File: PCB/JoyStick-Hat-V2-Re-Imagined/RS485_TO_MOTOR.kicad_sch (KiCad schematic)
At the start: 16 parts, among them J5 RJHSE-5381, U4 MAX3535ECWI+T

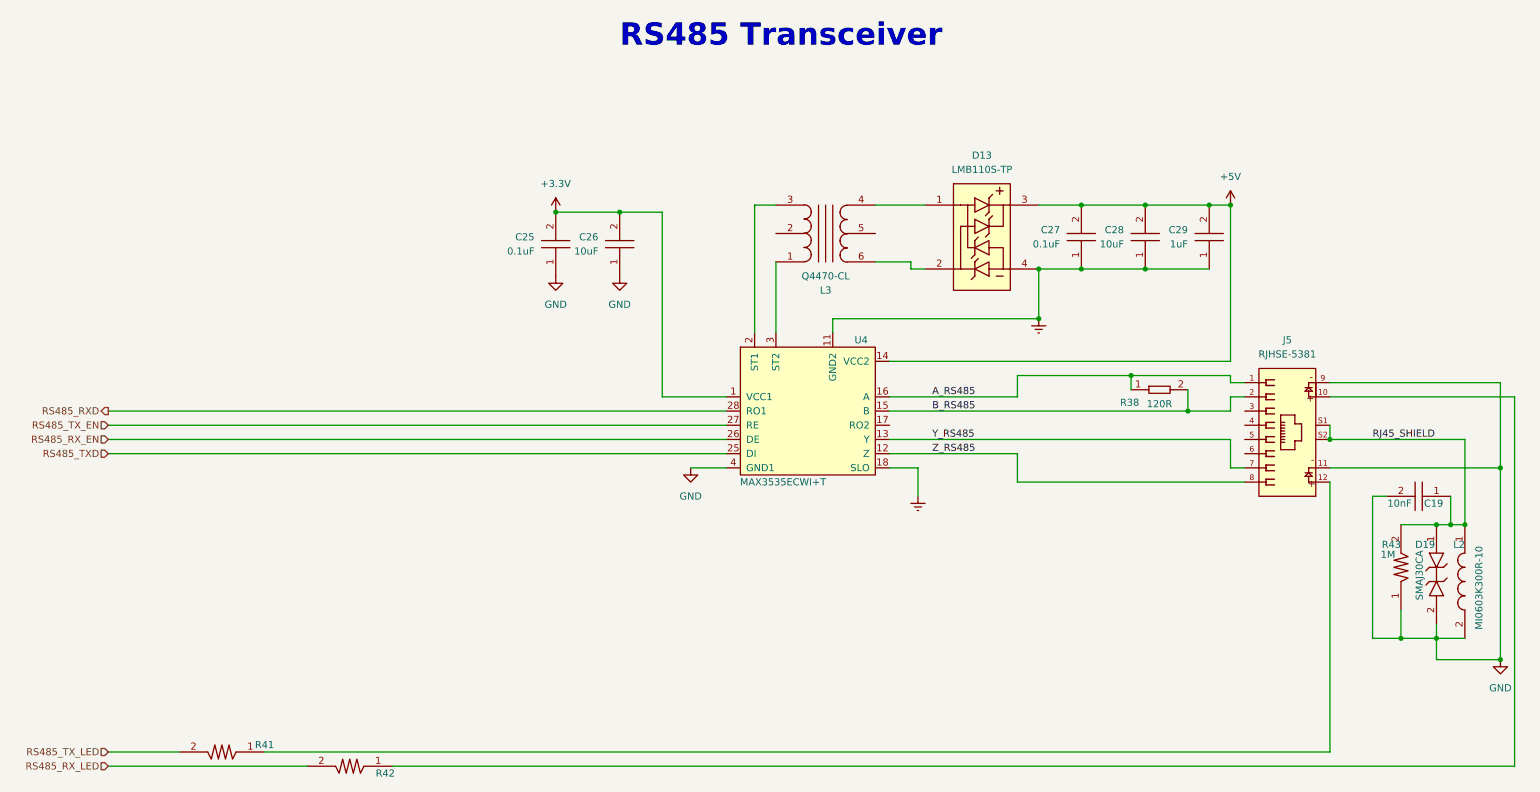
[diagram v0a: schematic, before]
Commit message: Daisy Chaining
Modified RS485 circuit with dual port connector for daisy chaining systems on the wheel chair !
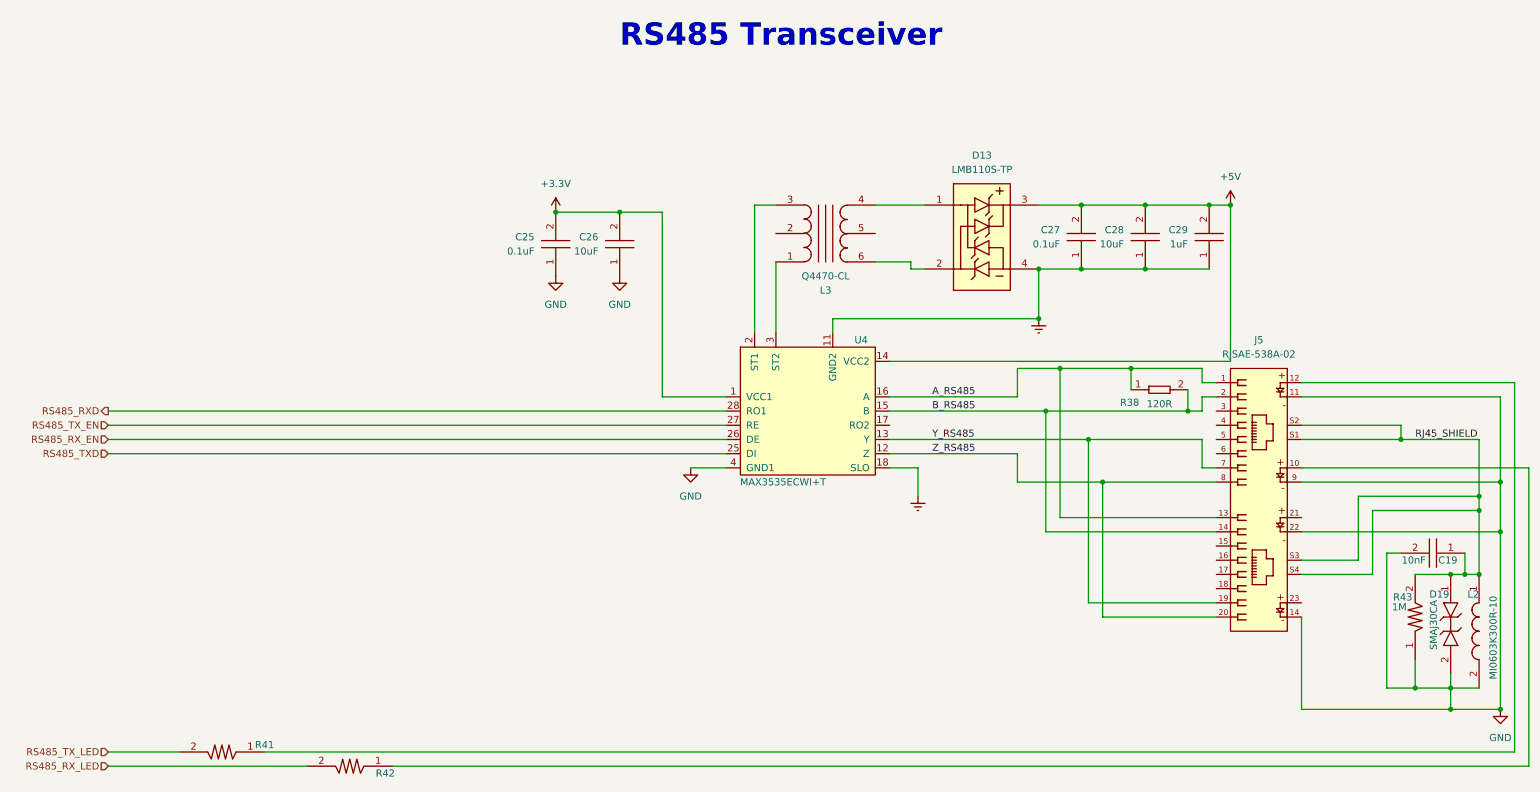
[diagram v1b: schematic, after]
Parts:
- removed J5: RJHSE-5381, AVR-KiCAD-Lib-Connectors:AMPHENOL_RJHSE-5381, symbol AVR-KiCAD-Lib-Connectors:RJHSE-5381
- added J5: RJSAE-538A-02, AVR-KiCAD-Lib-Connectors:AMPHENOL_RJSAE538A02, symbol AVR-KiCAD-Lib-Connectors:RJSAE-538A-02
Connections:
- net A_RS485: now also J5.1, J5.13
- net B_RS485: now also J5.14, J5.2
- net GND: now also J5.11, J5.14, J5.22, J5.9
- net RJ45_SHIELD: now also J5.S1, J5.S2, J5.S3, J5.S4
- net Y_RS485: now also J5.19, J5.7
- net Z_RS485: now also J5.20, J5.8
- net at R42.1: now also J5.10
- net at R41.1: now also J5.12
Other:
- moved on the sheet: C19, D19, L2, R43

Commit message: Fab Fixes
Fixing for Frabrication, DRC cleared by pending external review subject to change.
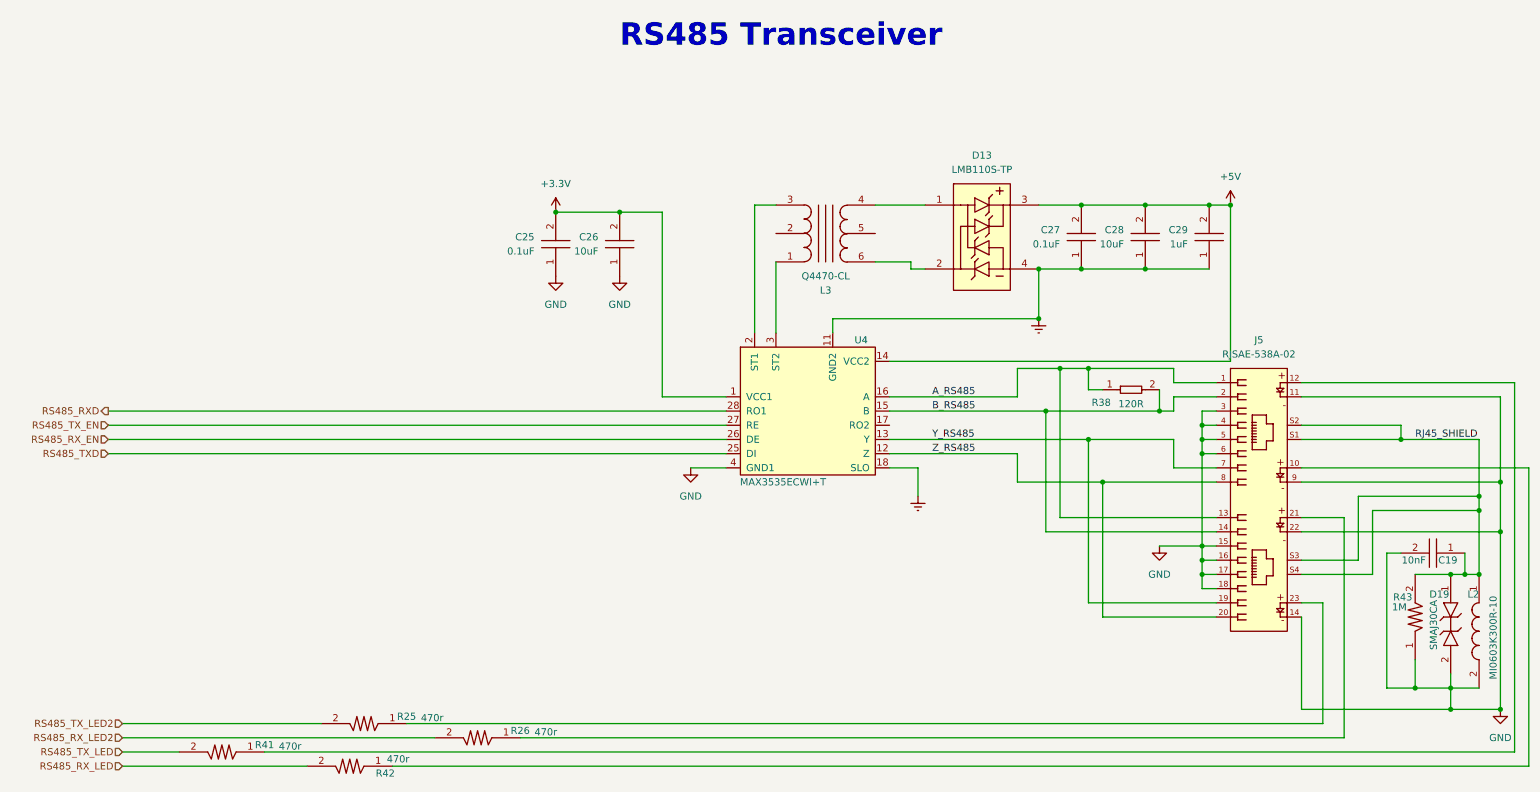
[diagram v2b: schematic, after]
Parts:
- added R25, R26: RC0603FR-07470RL, AVR-KiCAD-Lib-Resistors:R0603, symbol AVR-KiCAD-Lib-Resistors:RC0603FR-07470RL
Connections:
- net GND: now also J5.15, J5.16, J5.17, J5.18, J5.3, J5.4, J5.5, J5.6
- net at J5.21: now also R26.1
- net at J5.23: now also R25.1
- new net RS485_RX_LED2: R26.2
- new net RS485_TX_LED2: R25.2
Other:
- moved on the sheet: R38

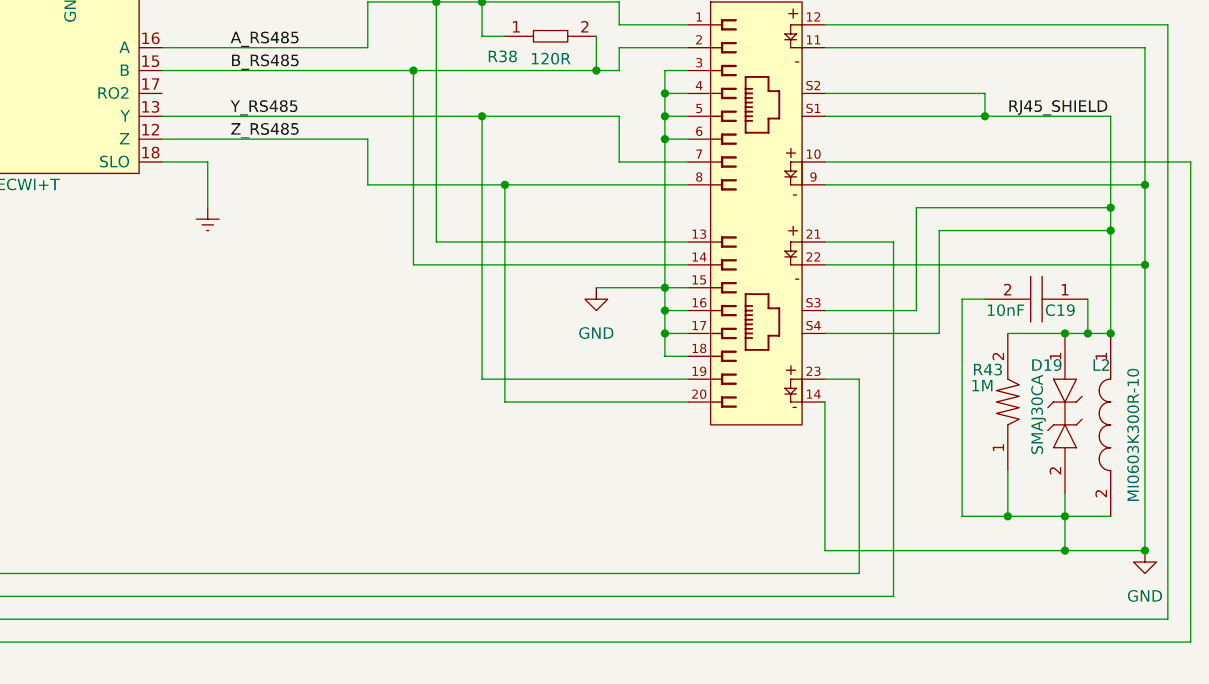
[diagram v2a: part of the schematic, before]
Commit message: RS485 Circuit Fixes, STM32 Expansion
Fixe RS485 circuit errors, changed PCB topology for RS485. Added STM32 expansion IO in place of 5V Regulator.
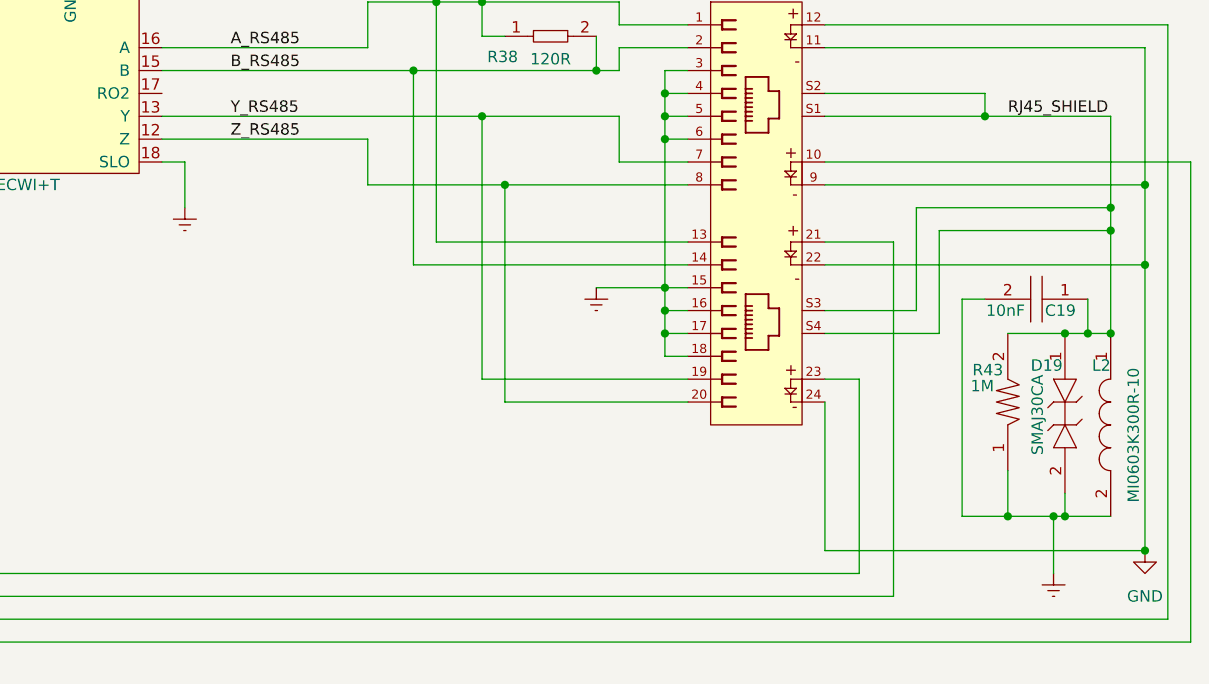
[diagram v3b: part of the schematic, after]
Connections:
- net Earth: now also C19.2, D19.2, J5.15, J5.16, J5.17, J5.18, J5.3, J5.4, J5.5, J5.6, L2.2, R43.1
- net GND: now also J5.24; no longer C19.2, D19.2, J5.14, J5.15, J5.16, J5.17, J5.18, J5.3, J5.4, J5.5, J5.6, L2.2, R43.1
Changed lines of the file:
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@@
 	)
 	(junction
+		(at 266.7 148.59)
+		(diameter 0)
+		(color 0 0 0 0)
+	)
+	(junction
 		(at 267.97 148.59)
 		(diameter 0)
@@
 	)
 	(junction
-		(at 267.97 152.4)
-		(diameter 0)
-		(color 0 0 0 0)
-	)
-	(junction
 		(at 119.38 63.5)
 		(diameter 0)
@@
 	(wire
 		(pts
-			(xy 241.3 152.4) (xy 267.97 152.4)
-		)
-		(stroke
-			(width 0)
-			(type default)
-		)
-	)
-	(wire
-		(pts
 			(xy 119.38 63.5) (xy 127 63.5)
 		)
@@
 	(wire
 		(pts
-			(xy 267.97 148.59) (xy 267.97 152.4)
-		)
-		(stroke
-			(width 0)
-			(type default)
-		)
-	)
-	(wire
-		(pts
 			(xy 213.36 62.23) (xy 224.79 62.23)
 		)
@@
 	(wire
 		(pts
-			(xy 167.64 109.22) (xy 172.72 109.22)
+			(xy 170.18 109.22) (xy 167.64 109.22)
 		)
 		(stroke
@@
 	(wire
 		(pts
-			(xy 267.97 148.59) (xy 261.62 148.59)
+			(xy 267.97 148.59) (xy 266.7 148.59)
 		)
 		(stroke
@@
 	(wire
 		(pts
+			(xy 266.7 148.59) (xy 266.7 154.94)
+		)
+		(stroke
+			(width 0)
+			(type default)
+		)
+	)
+	(wire
+		(pts
 			(xy 27.94 101.6) (xy 138.43 101.6)
 		)
@@
 	(wire
 		(pts
-			(xy 267.97 152.4) (xy 276.86 152.4)
+			(xy 241.3 152.4) (xy 276.86 152.4)
 		)
 		(stroke
@@
 	(wire
 		(pts
-			(xy 172.72 109.22) (xy 172.72 114.3)
+			(xy 170.18 109.22) (xy 170.18 114.3)
 		)
 		(stroke
@@
 	(wire
 		(pts
+			(xy 266.7 148.59) (xy 261.62 148.59)
+		)
+		(stroke
+			(width 0)
+			(type default)
+		)
+	)
+	(wire
+		(pts
 			(xy 190.5 106.68) (xy 190.5 111.76)
 		)
@@
 	(symbol
 		(lib_id "power:Earth")
-		(at 172.72 114.3 0)
+		(at 170.18 114.3 0)
 		(unit 1)
 		(exclude_from_sim no)
@@
 		(fields_autoplaced yes)
 		(property "Reference" "#PWR068"
-			(at 172.72 120.65 0)
+			(at 170.18 120.65 0)
 			(effects
 				(font
@@
 		)
 		(property "Value" "Earth"
-			(at 172.72 118.11 0)
+			(at 170.18 118.11 0)
 			(effects
 				(font
@@
 		)
 		(property "Footprint" ""
-			(at 172.72 114.3 0)
+			(at 170.18 114.3 0)
 			(effects
 				(font
@@
 		)
 		(property "Datasheet" "~"
-			(at 172.72 114.3 0)
+			(at 170.18 114.3 0)
 			(effects
 				(font
@@
 		)
 		(property "Description" ""
-			(at 172.72 114.3 0)
+			(at 170.18 114.3 0)
 			(effects
 				(font
@@
 		(pin "4"
 		)
-		(pin "14"
+		(pin "24"
 		)
 		(pin "7"
@@
 	)
 	(symbol
+		(lib_id "power:Earth")
+		(at 215.9 123.19 0)
+		(unit 1)
+		(exclude_from_sim no)
+		(in_bom yes)
+		(on_board yes)
+		(dnp no)
+		(fields_autoplaced yes)
+		(property "Reference" "#PWR038"
+			(at 215.9 129.54 0)
+			(effects
+				(font
+					(size 1.27 1.27)
+				)
+				(hide yes)
+			)
+		)
+		(property "Value" "Earth"
+			(at 215.9 127 0)
+			(effects
+				(font
+					(size 1.27 1.27)
+				)
+				(hide yes)
+			)
+		)
+		(property "Footprint" ""
+			(at 215.9 123.19 0)
+			(effects
+				(font
+					(size 1.27 1.27)
+				)
+				(hide yes)
+			)
+		)
+		(property "Datasheet" "~"
+			(at 215.9 123.19 0)
+			(effects
+				(font
+					(size 1.27 1.27)
+				)
+				(hide yes)
+			)
+		)
+		(property "Description" ""
+			(at 215.9 123.19 0)
+			(effects
+				(font
+					(size 1.27 1.27)
+				)
+				(hide yes)
+			)
+		)
+		(pin "1"
+		)
+		(instances
+			(project "JoyStick-Hat-V2-Re-Imagined"
+				(path "/cf0c81b5-5bdf-47c3-83c0-f6980f515e65/82e1f9af-1e5c-4e7f-8d36-34a266d2a8ff"
+					(reference "#PWR038")
+					(unit 1)
+				)
+			)
+		)
+	)
+	(symbol
 		(lib_id "AVR-KiCAD-Lib-Capacitors:CGA5L3X5R1V106K160AB")
 		(at 119.38 69.85 90)
@@
 	)
 	(symbol
+		(lib_id "power:Earth")
+		(at 266.7 154.94 0)
+		(unit 1)
+		(exclude_from_sim no)
+		(in_bom yes)
+		(on_board yes)
+		(dnp no)
+		(fields_autoplaced yes)
+		(property "Reference" "#PWR041"
+			(at 266.7 161.29 0)
+			(effects
+				(font
+					(size 1.27 1.27)
+				)
+				(hide yes)
+			)
+		)
+		(property "Value" "Earth"
+			(at 266.7 158.75 0)
+			(effects
+				(font
+					(size 1.27 1.27)
+				)
+				(hide yes)
+			)
+		)
+		(property "Footprint" ""
+			(at 266.7 154.94 0)
+			(effects
+				(font
+					(size 1.27 1.27)
+				)
+				(hide yes)
+			)
+		)
+		(property "Datasheet" "~"
+			(at 266.7 154.94 0)
+			(effects
+				(font
+					(size 1.27 1.27)
+				)
+				(hide yes)
+			)
+		)
+		(property "Description" ""
+			(at 266.7 154.94 0)
+			(effects
+				(font
+					(size 1.27 1.27)
+				)
+				(hide yes)
+			)
+		)
+		(pin "1"
+		)
+		(instances
+			(project "JoyStick-Hat-V2-Re-Imagined"
+				(path "/cf0c81b5-5bdf-47c3-83c0-f6980f515e65/82e1f9af-1e5c-4e7f-8d36-34a266d2a8ff"
+					(reference "#PWR041")
+					(unit 1)
+				)
+			)
+		)
+	)
+	(symbol
 		(lib_id "AVR-KiCAD-Lib-Resistors:RC1206FR-071ML")
 		(at 261.62 135.89 270)
@@
 					(unit 1)
 				)
-			)
-		)
-	)
-	(symbol
-		(lib_id "power:GND")
-		(at 215.9 123.19 0)
-		(unit 1)
-		(exclude_from_sim no)
-		(in_bom yes)
-		(on_board yes)
-		(dnp no)
-		(fields_autoplaced yes)
-		(property "Reference" "#PWR044"
-			(at 215.9 129.54 0)
-			(effects
-				(font
-					(size 1.27 1.27)
-				)
-				(hide yes)
-			)
-		)
-		(property "Value" "GND"
-			(at 215.9 128.27 0)
-			(effects
-				(font
-					(size 1.27 1.27)
-				)
-			)
-		)
-		(property "Footprint" ""
-			(at 215.9 123.19 0)
-			(effects
-				(font
-					(size 1.27 1.27)
-				)
-				(hide yes)
-			)
-		)
-		(property "Datasheet" ""
-			(at 215.9 123.19 0)
-			(effects
-				(font
-					(size 1.27 1.27)
-				)
-				(hide yes)
-			)
-		)
-		(property "Description" ""
-			(at 215.9 123.19 0)
-			(effects
-				(font
-					(size 1.27 1.27)
-				)
-				(hide yes)
-			)
-		)
-		(pin "1"
-		)
-		(instances
-			(project "JoyStick-Hat-V2-Re-Imagined"
-				(path "/cf0c81b5-5bdf-47c3-83c0-f6980f515e65/82e1f9af-1e5c-4e7f-8d36-34a266d2a8ff"
-					(reference "#PWR044")
-					(unit 1)
-				)
